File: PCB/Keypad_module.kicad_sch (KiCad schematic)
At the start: 50 parts, among them J3 Conn_01x06_Pin, SW100 SW_Push, SW101 SW_Push, SW102 SW_Push, SW83 SW_Push, SW84 SW_Push, SW85 SW_Push, SW86 SW_Push, SW87 SW_Push, SW88 SW_Push, SW89 SW_Push, SW90 SW_Push, SW91 SW_Push, SW92 SW_Push, SW93 SW_Push, SW94 SW_Push, SW95 SW_Push, SW96 SW_Push, SW97 SW_Push, SW98 SW_Push, SW99 SW_Push, U6 XIAO-nRF52840-SMD, U7 MCP23017_ML

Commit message: Added Keypad module
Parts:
- removed J3: Conn_01x06_Pin, Connector_PinHeader_1.00mm:PinHeader_1x06_P1.00mm_Vertical, symbol Connector:Conn_01x06_Pin
- added Brd11, Brd12: SSD1306, Footprints:128x64OLED, symbol SSD1306-128x64_OLED:SSD1306
- added C12: 0.1uF, Capacitor_SMD:C_0805_2012Metric, symbol Device:C
- added C13: 10uF, Capacitor_SMD:C_0805_2012Metric, symbol Device:C
- added Conn5, Conn6, Conn7, Conn8: Conn_01x06_Pin, Connector_PinHeader_2.54mm:PinHeader_1x06_P2.54mm_Vertical, symbol Connector:Conn_01x06_Pin
- added D186, D187, D188, D189, D190, D191, D192, D193, D194, D195, D196, D197, D198, D199, D200, D201, D202, D203, D204, D205: SK6805, LED_SMD:LED_SK6805_PLCC4_2.4x2.7mm_P1.3mm, symbol LED:SK6805
- added D206: ESDA5V3L, Package_TO_SOT_SMD:SOT-23-3, symbol Power_Protection:ESDA5V3L
- added R23: 24K9, Resistor_SMD:R_0805_2012Metric, symbol Device:R
- added R24, R27: 10K, Resistor_SMD:R_0805_2012Metric, symbol Device:R
- added R25: 34K8, Resistor_SMD:R_0805_2012Metric, symbol Device:R
- added R26: 20K, Resistor_SMD:R_0805_2012Metric, symbol Device:R
- added U13: LTC4217, DFN-16_DHC_LIT:DFN-16_DHC_LIT, symbol Custom Symbols:LTC4217
- U6: footprint a:modified-XIAO-nRF52840-SMD -> Footprints:modified-XIAO-nRF52840-SMD
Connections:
- net GND: now also Brd11.1 (GND), Brd12.1 (GND), C12.2, C13.2, Conn5.6 (Pin_6), Conn6.6 (Pin_6), Conn7.6 (Pin_6), Conn8.6 (Pin_6), D186.2 (VSS), D187.2 (VSS), D188.2 (VSS), D189.2 (VSS), D190.2 (VSS), D191.2 (VSS), D192.2 (VSS), D193.2 (VSS), D194.2 (VSS), D195.2 (VSS), D196.2 (VSS), D197.2 (VSS), D198.2 (VSS), D199.2 (VSS), D200.2 (VSS), D201.2 (VSS), D202.2 (VSS), D203.2 (VSS), D204.2 (VSS), D205.2 (VSS), D206.3 (A), R24.1, R26.2, R27.2, U13.17 (GND), U13.6 (GND)
- net K3V3: now also U7.5 (VDD), Brd11.2 (VCC), Brd12.2 (VCC)
- net KBT_PIN: now also U6.2 (P0.03_A1_D1); no longer U6.1 (P0.02_A0_D0)
- net KCOL0: now also U7.22 (GPA5); no longer U7.25 (GPB0)
- net KCOL1: now also U7.23 (GPA6); no longer U7.26 (GPB1)
- net KCOL2: now also U7.24 (GPA7); no longer U7.27 (GPB2)
- net KCOL3: now also U7.25 (GPB0); no longer U7.28 (GPB3)
- net KMCP_RESET: now also U6.8 (P1.12_D7_RX); no longer U6.7 (P1.11_D6_TX)
- net KSCL: now also Brd11.3 (SCL), Brd12.3 (SCL), Conn5.2 (Pin_2), Conn6.2 (Pin_2), Conn7.2 (Pin_2), Conn8.2 (Pin_2), D206.1 (K)
- net KSDA: now also Brd11.4 (SDA), Brd12.4 (SDA), Conn5.3 (Pin_3), Conn6.3 (Pin_3), Conn7.3 (Pin_3), Conn8.3 (Pin_3), D206.2 (K)
- net KID3: now reaches U7.1 (GPB4)
- net KID3: now also Conn7.5 (Pin_5)
- net KINT3: now reaches U7.2 (GPB5)
- net KINT3: now also Conn7.4 (Pin_4)
- net KINT2: now reaches U7.3 (GPB6)
- net KINT2: now also Conn6.4 (Pin_4)
- net KID2: now reaches U7.4 (GPB7)
- net KID2: now also Conn6.5 (Pin_5)
- net VDD: now reaches U6.14 (5V)
- net VDD: now also D186.4 (VDD), D187.4 (VDD), D188.4 (VDD), D189.4 (VDD), D190.4 (VDD), D191.4 (VDD), D192.4 (VDD), D193.4 (VDD), D194.4 (VDD), D195.4 (VDD), D196.4 (VDD), D197.4 (VDD), D198.4 (VDD), D199.4 (VDD), D200.4 (VDD), D201.4 (VDD), D202.4 (VDD), D203.4 (VDD), D204.4 (VDD), D205.4 (VDD), R23.1, R25.1, U13.1 (VDD), U13.16 (VDD)
- net KVB_EN: now reaches U6.3 (P0.28_A2_D2)
- net KVB_EN: now also R23.2, R24.2, U13.2 (UV)
- net KFLT: now reaches U6.4 (P0.29_A3_D3)
- net KFLT: now also U13.12 (FLT)
- net KCOM renamed KID1
- net KID1: now also Conn5.5 (Pin_5)
- net KPRESENCE renamed KINT1
- net KINT1: now also Conn5.4 (Pin_4)
- new net: D190.1 (DOUT), D194.3 (DIN)
- new net: D190.3 (DIN), D191.1 (DOUT)
- new net: D198.3 (DIN), D199.1 (DOUT)
- new net: D199.3 (DIN), D200.1 (DOUT)
- new net: D191.3 (DIN), D192.1 (DOUT)
- new net: D192.3 (DIN), D193.1 (DOUT)
- new net: R25.2, R27.1, U13.3 (OV)
- new net: D203.1 (DOUT), D204.3 (DIN)
- new net: D202.1 (DOUT), D203.3 (DIN)
- new net: D204.1 (DOUT), D205.3 (DIN)
- new net: D198.1 (DOUT), D202.3 (DIN)
- new net: D200.3 (DIN), D201.1 (DOUT)
- new net: D197.1 (DOUT), D201.3 (DIN)
- new net: D196.1 (DOUT), D197.3 (DIN)
- new net: D195.1 (DOUT), D196.3 (DIN)
- new net: D189.1 (DOUT), D193.3 (DIN)
- new net: D188.1 (DOUT), D189.3 (DIN)
- new net: D187.1 (DOUT), D188.3 (DIN)
- new net: D186.1 (DOUT), D187.3 (DIN)
- new net: D194.1 (DOUT), D195.3 (DIN)
- new net: C12.1, U13.10 (GATE)
- new net: R26.1, U13.15 (I_SET)
- new net: C13.1, U13.4 (TIMER), U13.5 (INTV_CC)
- new net KID4: Conn8.5 (Pin_5), U7.28 (GPB3)
- new net KINT4: Conn8.4 (Pin_4), U7.27 (GPB2)
- new net KLEDs: D186.3 (DIN), U6.7 (P1.11_D6_TX)
- new net KV_SW: Conn5.1 (Pin_1), Conn6.1 (Pin_1), Conn7.1 (Pin_1), Conn8.1 (Pin_1), U13.13 (FB), U13.7 (OUT), U13.8 (OUT), U13.9 (OUT)
- no-connect marks 24 -> 15
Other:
- moved on the sheet: R15, R16, TP3, TP4

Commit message: Add: Production files
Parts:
- Brd11, Brd12: value SSD1306 -> SH1106; Link (none) -> https://www.aliexpress.com/item/1005009242613187.html; Name (none) -> OLED Screen; Shipping (none) -> $0.99; Unit Price ($) (none) -> 1.89
- C12: Comment C49678 -> (none); LCSC Part # (none) -> C49678; Link (none) -> https://jlcpcb.com/partdetail/C49678; Unit Price ($) (none) -> 0.01
- C13: Comment C15850 -> (none); LCSC Part # (none) -> C15850; Link (none) -> https://jlcpcb.com/partdetail/C15850; Name (none) -> Capacitors; Unit Price ($) (none) -> 0.01
- Conn5, Conn6, Conn7, Conn8: Link (none) -> https://www.aliexpress.com/item/1005007636554292.html; Name (none) -> 1X6 Magnetic Pogo Pins; Shipping (none) -> $4.65; Unit Price ($) (none) -> 1.84
- D100, D101, D102, D103, D84, D85, D86, D87, D88, D89, D90, D91, D92, D93, D94, D95, D96, D97, D98, D99: LCSC Part # (none) -> C2099; Link (none) -> https://jlcpcb.com/partdetail/C2099; Name (none) -> Diodes; Unit Price ($) (none) -> 0.01; now in the parts list
- D186, D187, D188, D189, D190, D191, D192, D193, D194, D195, D196, D197, D198, D199, D200, D201, D202, D203, D204, D205: Comment C2890035 -> (none); LCSC Part # (none) -> C2890035; Link (none) -> https://jlcpcb.com/partdetail/C2890035; Name (none) -> SK6805 (LEDs); Unit Price ($) (none) -> 0.10
- D206: Comment C587142 -> (none); LCSC Part # (none) -> C587142; Link (none) -> https://jlcpcb.com/partdetail/C587142; Name (none) -> ESDA5V3L (ESD protector for I2C lines); Unit Price ($) (none) -> 0.04
- R14: value 10kΩ -> 10K; LCSC Part # (none) -> C17414; Link (none) -> https://jlcpcb.com/partdetail/C17414; Unit Price ($) (none) -> 0.01; now in the parts list
- R15: value 806kΩ -> 806K; LCSC Part # (none) -> C2933502; Link (none) -> https://jlcpcb.com/partdetail/C2933502; Unit Price ($) (none) -> 0.01; now in the parts list
- R16: value 2MΩ -> 2M; LCSC Part # (none) -> C26112; Link (none) -> https://jlcpcb.com/partdetail/C26112; Unit Price ($) (none) -> 0.01; now in the parts list
- R17, R18: value 4.7kΩ -> 4K7; LCSC Part # (none) -> C17673; Link (none) -> https://jlcpcb.com/partdetail/C17673; Unit Price ($) (none) -> 0.01; now in the parts list
- R23: Comment C17571 -> (none); LCSC Part # (none) -> C17571; Link (none) -> https://jlcpcb.com/partdetail/C17571; Unit Price ($) (none) -> 0.01
- R24, R27: Comment C17414 -> (none); LCSC Part # (none) -> C17414; Link (none) -> https://jlcpcb.com/partdetail/C17414; Unit Price ($) (none) -> 0.01
- R25: Comment C2933423 -> (none); LCSC Part # (none) -> C2933423; Link (none) -> https://jlcpcb.com/partdetail/C2933423; Unit Price ($) (none) -> 0.01
- R26: Comment C4328 -> (none); LCSC Part # (none) -> C4328; Link (none) -> https://jlcpcb.com/partdetail/C4328; Unit Price ($) (none) -> 0.01
- SW100, SW101, SW102, SW83, SW84, SW85, SW86, SW87, SW88, SW89, SW90, SW91, SW92, SW93, SW94, SW95, SW96, SW97, SW98, SW99: LCSC Part # (none) -> C5333465; Link (none) -> https://jlcpcb.com/partdetail/C5333465; Name (none) -> Keys; Unit Price ($) (none) -> 0.1213; moq (none) -> 73; now in the parts list
- U13: Comment C687462 -> (none); LCSC Part # (none) -> C687462; Link (none) -> https://jlcpcb.com/partdetail/C687462; Name (none) -> LTC4217 (Hotswap-controller); Unit Price ($) (none) -> 11.90
- U6: LCSC Part # (none) -> C37327670; Link (none) -> https://jlcpcb.com/partdetail/C37327670; Name (none) -> XIAO-nRF52840-SMD (MCU); Unit Price ($) (none) -> 0.0196; moq (none) -> 447; now in the parts list
- U7: LCSC Part # (none) -> C639770; Link (none) -> https://jlcpcb.com/partdetail/C639770; Name (none) -> MCP23017 (GPIO expander); Unit Price ($) (none) -> 1.93; now in the parts list
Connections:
- net KCOL2: now also U7.25 (GPB0); no longer U7.24 (GPA7)
- net KCOL3: now also U7.26 (GPB1); no longer U7.25 (GPB0)
- net KID2: now also U7.3 (GPB6); no longer U7.4 (GPB7)
- net KINT2: now also U7.4 (GPB7); no longer U7.3 (GPB6)

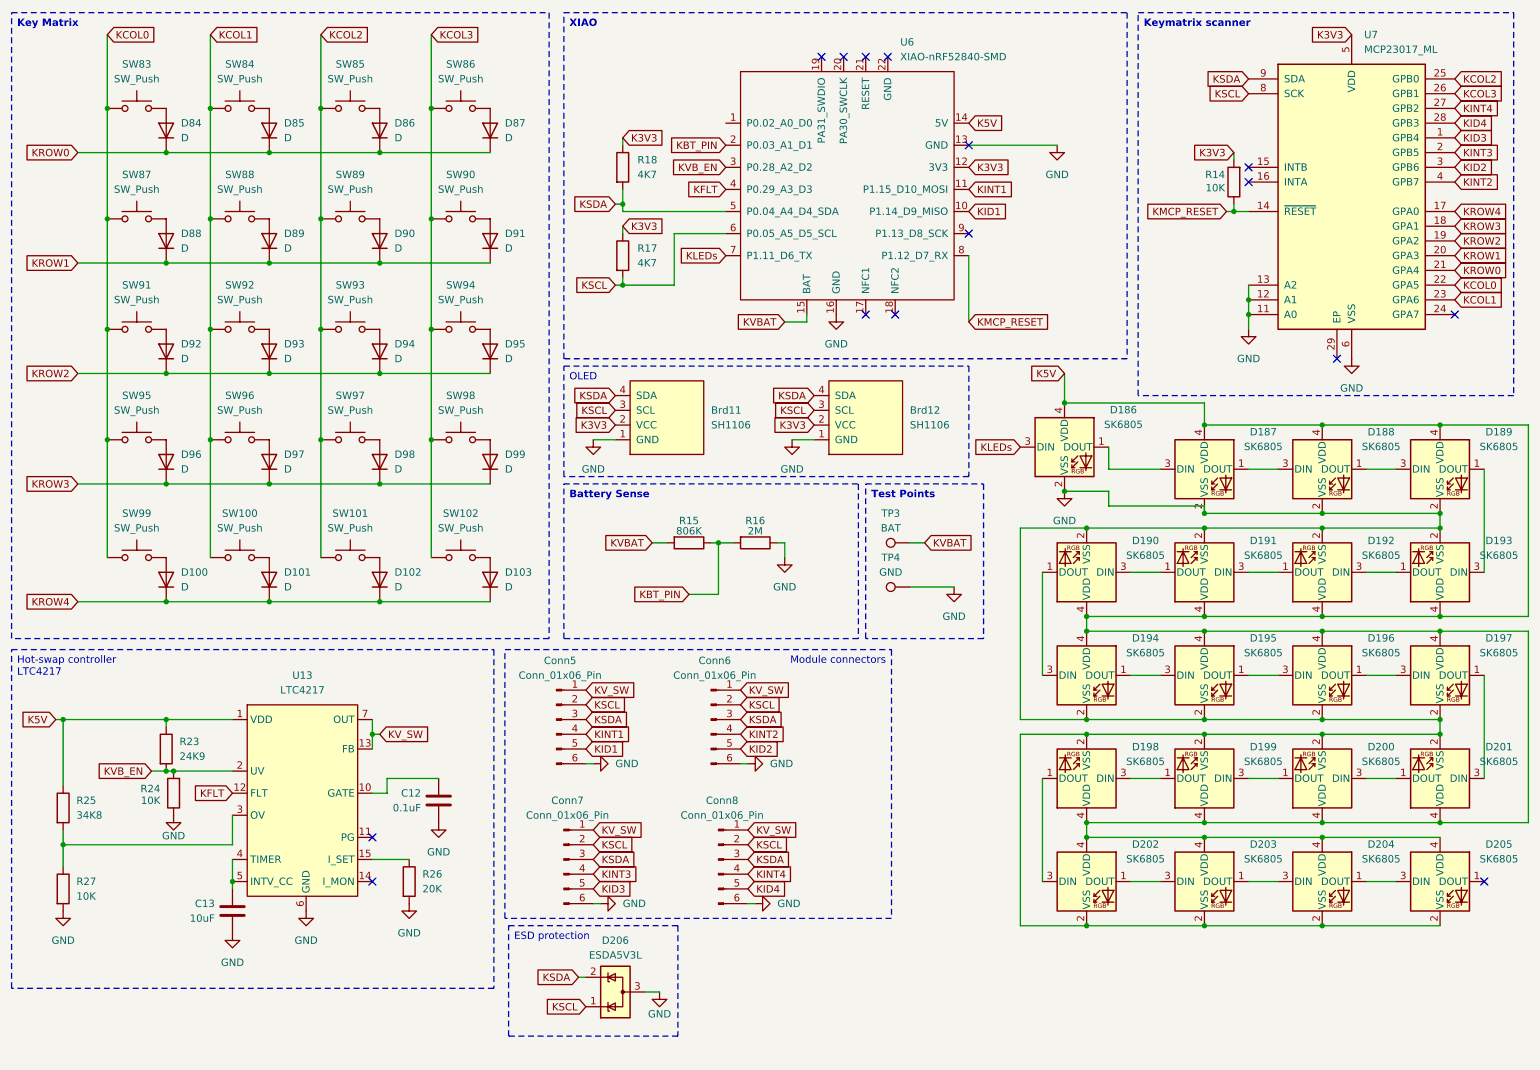
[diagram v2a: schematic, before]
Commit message: Simplified design to reduce cost
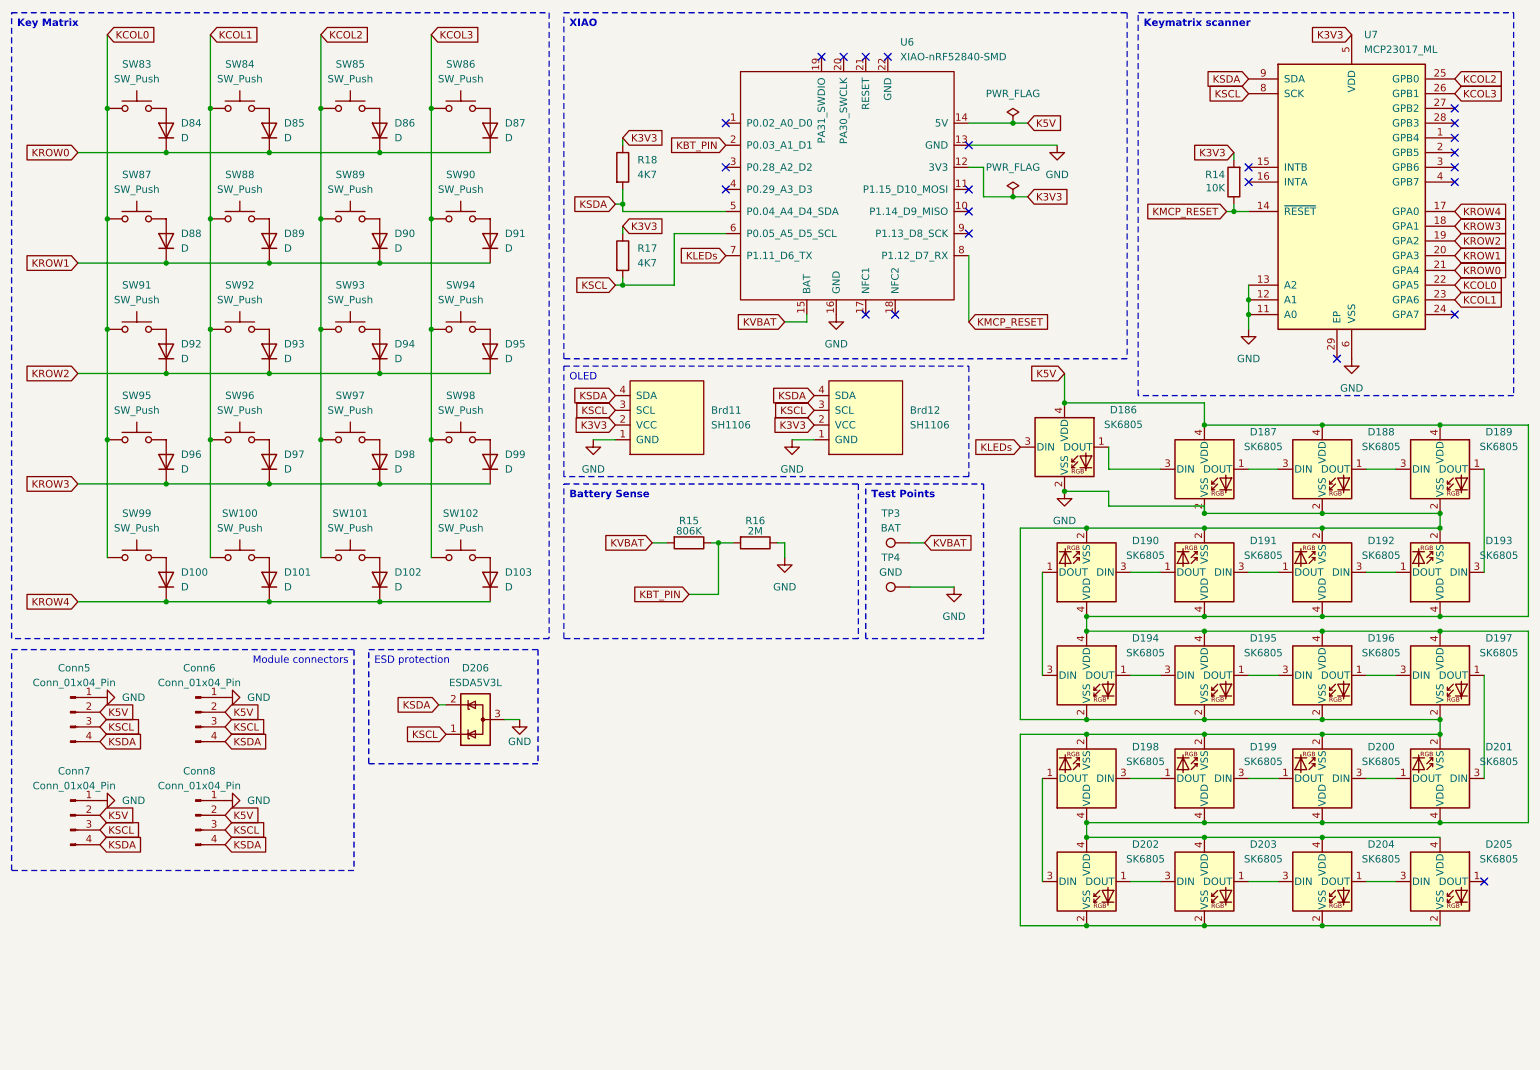
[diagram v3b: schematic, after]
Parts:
- removed C12: 0.1uF, Capacitor_SMD:C_0805_2012Metric, symbol Device:C
- removed C13: 10uF, Capacitor_SMD:C_0805_2012Metric, symbol Device:C
- removed Conn5, Conn6, Conn7, Conn8: Conn_01x06_Pin, Connector_PinHeader_2.54mm:PinHeader_1x06_P2.54mm_Vertical, symbol Connector:Conn_01x06_Pin
- removed R23: 24K9, Resistor_SMD:R_0805_2012Metric, symbol Device:R
- removed R24, R27: 10K, Resistor_SMD:R_0805_2012Metric, symbol Device:R
- removed R25: 34K8, Resistor_SMD:R_0805_2012Metric, symbol Device:R
- removed R26: 20K, Resistor_SMD:R_0805_2012Metric, symbol Device:R
- removed U13: LTC4217, DFN-16_DHC_LIT:DFN-16_DHC_LIT, symbol Custom Symbols:LTC4217
- added Conn5, Conn6, Conn7, Conn8: Conn_01x04_Pin, Connector_PinHeader_2.54mm:PinHeader_1x04_P2.54mm_Vertical, symbol Connector:Pogopin_connector_01x04
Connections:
- net GND: now also Conn5.1 (Pin_1), Conn6.1 (Pin_1), Conn7.1 (Pin_1), Conn8.1 (Pin_1)
- net KSCL: now also Conn5.3 (Pin_3), Conn6.3 (Pin_3), Conn7.3 (Pin_3), Conn8.3 (Pin_3)
- net KSDA: now also Conn5.4 (Pin_4), Conn6.4 (Pin_4), Conn7.4 (Pin_4), Conn8.4 (Pin_4)
- net KFLT: no longer names the net of U6.4 (P0.29_A3_D3)
- net KID1: no longer names the net of U6.10 (P1.14_D9_MISO)
- net KID2: no longer names the net of U7.3 (GPB6)
- net KID3: no longer names the net of U7.1 (GPB4)
- net KID4: no longer names the net of U7.28 (GPB3)
- net KINT1: no longer names the net of U6.11 (P1.15_D10_MOSI)
- net KINT2: no longer names the net of U7.4 (GPB7)
- net KINT3: no longer names the net of U7.2 (GPB5)
- net KINT4: no longer names the net of U7.27 (GPB2)
- net KVB_EN: no longer names the net of U6.3 (P0.28_A2_D2)
- net VDD renamed K5V
- net K5V: now also Conn5.2 (Pin_2), Conn6.2 (Pin_2), Conn7.2 (Pin_2), Conn8.2 (Pin_2)
- no-connect marks 15 -> 24
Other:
- moved on the sheet: D206

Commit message: Update: Schematic and mainboard PCB
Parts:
- removed D101, D103, D95: D, Diode_SMD:D_SOD-123, symbol Device:D
- removed D186, D187, D188, D189, D190, D191, D192, D193, D194, D195, D196, D197, D198, D199, D200, D201, D202, D203, D204, D205: SK6805, LED_SMD:LED_SK6805_PLCC4_2.4x2.7mm_P1.3mm, symbol LED:SK6805
- removed SW100, SW102, SW94: SW_Push, PCM_marbastlib-choc:SW_choc_v1_HS_CPG135001S30_1u, symbol Switch:SW_Push
- added LED83, LED84, LED85, LED86, LED87, LED88, LED89, LED90, LED91, LED92, LED93, LED94, LED95, LED96, LED97, LED98, LED99: SK6803MINI-E, Footprints:LED, symbol ggxxacpy:SK6803MINI-E
- SW83, SW84, SW85, SW86, SW87, SW88, SW89, SW91, SW92, SW93: footprint PCM_marbastlib-choc:SW_choc_v1_HS_CPG135001S30_1u -> Footprints:Kailh_choc_HS_V2_1u
- SW90: footprint PCM_marbastlib-choc:SW_choc_v1_HS_CPG135001S30_1u -> Footprints:Kailh_choc_HS_V2_2u_90deg
- SW94: renamed from SW95; footprint PCM_marbastlib-choc:SW_choc_v1_HS_CPG135001S30_1u -> Footprints:Kailh_choc_HS_V2_1u
- SW95: renamed from SW96; footprint PCM_marbastlib-choc:SW_choc_v1_HS_CPG135001S30_1u -> Footprints:Kailh_choc_HS_V2_1u
- SW96: renamed from SW97; footprint PCM_marbastlib-choc:SW_choc_v1_HS_CPG135001S30_1u -> Footprints:Kailh_choc_HS_V2_1u
- SW97: renamed from SW98; footprint PCM_marbastlib-choc:SW_choc_v1_HS_CPG135001S30_1u -> Footprints:Kailh_choc_HS_V2_2u_90deg
- SW98: renamed from SW99; footprint PCM_marbastlib-choc:SW_choc_v1_HS_CPG135001S30_1u -> Footprints:Kailh_choc_HS_V2_2u
- SW99: renamed from SW101; footprint PCM_marbastlib-choc:SW_choc_v1_HS_CPG135001S30_1u -> Footprints:Kailh_choc_HS_V2_1u
- renumbered Brd11 to Brd1, Brd12 to Brd2, D84 to D83, D85 to D84, D86 to D85, D87 to D86, D88 to D87, D89 to D88, D90 to D89, D91 to D90, D92 to D91, D93 to D92, D94 to D93, D96 to D94, D97 to D95, D98 to D96, D99 to D97, D100 to D98, D102 to D99, D206 to ESD2, R14 to R19, R17 to R20, R15 to R21, R16 to R22, U6 to U5, U7 to U6
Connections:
- net GND: now also LED83.4 (VSS), LED84.4 (VSS), LED85.4 (VSS), LED86.4 (VSS), LED87.4 (VSS), LED88.4 (VSS), LED89.4 (VSS), LED90.4 (VSS), LED91.4 (VSS), LED92.4 (VSS), LED93.4 (VSS), LED94.4 (VSS), LED95.4 (VSS), LED96.4 (VSS), LED97.4 (VSS), LED98.4 (VSS), LED99.4 (VSS)
- net K5V: now also LED83.1 (VDD), LED84.1 (VDD), LED85.1 (VDD), LED86.1 (VDD), LED87.1 (VDD), LED88.1 (VDD), LED89.1 (VDD), LED90.1 (VDD), LED91.1 (VDD), LED92.1 (VDD), LED93.1 (VDD), LED94.1 (VDD), LED95.1 (VDD), LED96.1 (VDD), LED97.1 (VDD), LED98.1 (VDD), LED99.1 (VDD)
- net KLEDs: now also LED83.2 (DOUT)
- net KSCL: now also Conn5.4 (Pin_4), Conn6.4 (Pin_4), Conn7.4 (Pin_4), Conn8.4 (Pin_4); no longer Conn5.3 (Pin_3), Conn6.3 (Pin_3), Conn7.3 (Pin_3), Conn8.3 (Pin_3)
- net KSDA: now also Conn5.3 (Pin_3), Conn6.3 (Pin_3), Conn7.3 (Pin_3), Conn8.3 (Pin_3); no longer Conn5.4 (Pin_4), Conn6.4 (Pin_4), Conn7.4 (Pin_4), Conn8.4 (Pin_4)
- new net: LED96.3 (DIN), LED97.2 (DOUT)
- new net: LED97.3 (DIN), LED98.2 (DOUT)
- new net: LED85.3 (DIN), LED86.2 (DOUT)
- new net: LED86.3 (DIN), LED87.2 (DOUT)
- new net: LED90.3 (DIN), LED91.2 (DOUT)
- new net: LED91.3 (DIN), LED92.2 (DOUT)
- new net: LED95.3 (DIN), LED96.2 (DOUT)
- new net: LED94.3 (DIN), LED95.2 (DOUT)
- new net: LED88.3 (DIN), LED89.2 (DOUT)
- new net: LED89.3 (DIN), LED90.2 (DOUT)
- new net: LED87.3 (DIN), LED88.2 (DOUT)
- new net: LED83.3 (DIN), LED84.2 (DOUT)
- new net: LED84.3 (DIN), LED85.2 (DOUT)
- new net: LED93.3 (DIN), LED94.2 (DOUT)
- new net: LED92.3 (DIN), LED93.2 (DOUT)
- new net: LED98.3 (DIN), LED99.2 (DOUT)
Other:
- moved on the sheet: Conn5, Conn6, Conn7, Conn8, ESD2, R21, R22, TP3, TP4
